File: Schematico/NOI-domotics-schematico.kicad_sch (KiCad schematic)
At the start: 4 parts

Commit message: avanzo
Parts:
- added U?: (no value), symbol USB_5V:USB_DCconverter
- added U?: (no value), symbol Isolator:VO615A-4
- K?: value FINDER-34.51 -> (none)
- U?: value VO615A-4 -> (none)
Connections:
- net at U?. (VCC): now also J?.37 (GPIO26)
- net at J?.18 (GPIO24): now also U?. (VCC)
- net at J?.19 (GPIO10): now also U?. (VCC)
- net at J?.21 (GPIO9): now also U?. (VCC)
- net at J?.22 (GPIO25): now also U?. (VCC)
- net at J?.23 (GPIO11): now also U?. (VCC)
- net at J?.24 (GPIO8): now also U?. (VCC)
- net at J?.26 (GPIO7): now also U?. (VCC)
- net at J?.29 (GPIO5): now also U?. (VCC)
- net at J?.31 (GPIO6): now also U?. (VCC)
- net at J?.32 (GPIO12): now also U?. (VCC)
- net at J?.33 (GPIO13): now also U?. (VCC)
- net at J?.35 (GPIO19): now also U?. (VCC)
- net at J?.36 (GPIO16): now also U?. (VCC)
- net at J?.38 (GPIO20): now also U?. (VCC)
- net at J?.40 (GPIO21): now also U?. (VCC)
- net at K?. (VCC): now also U?.1 (VP)
- new net: K?. (VCC), U?.1 (VP) (x15)
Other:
- moved on the sheet: J?, U?

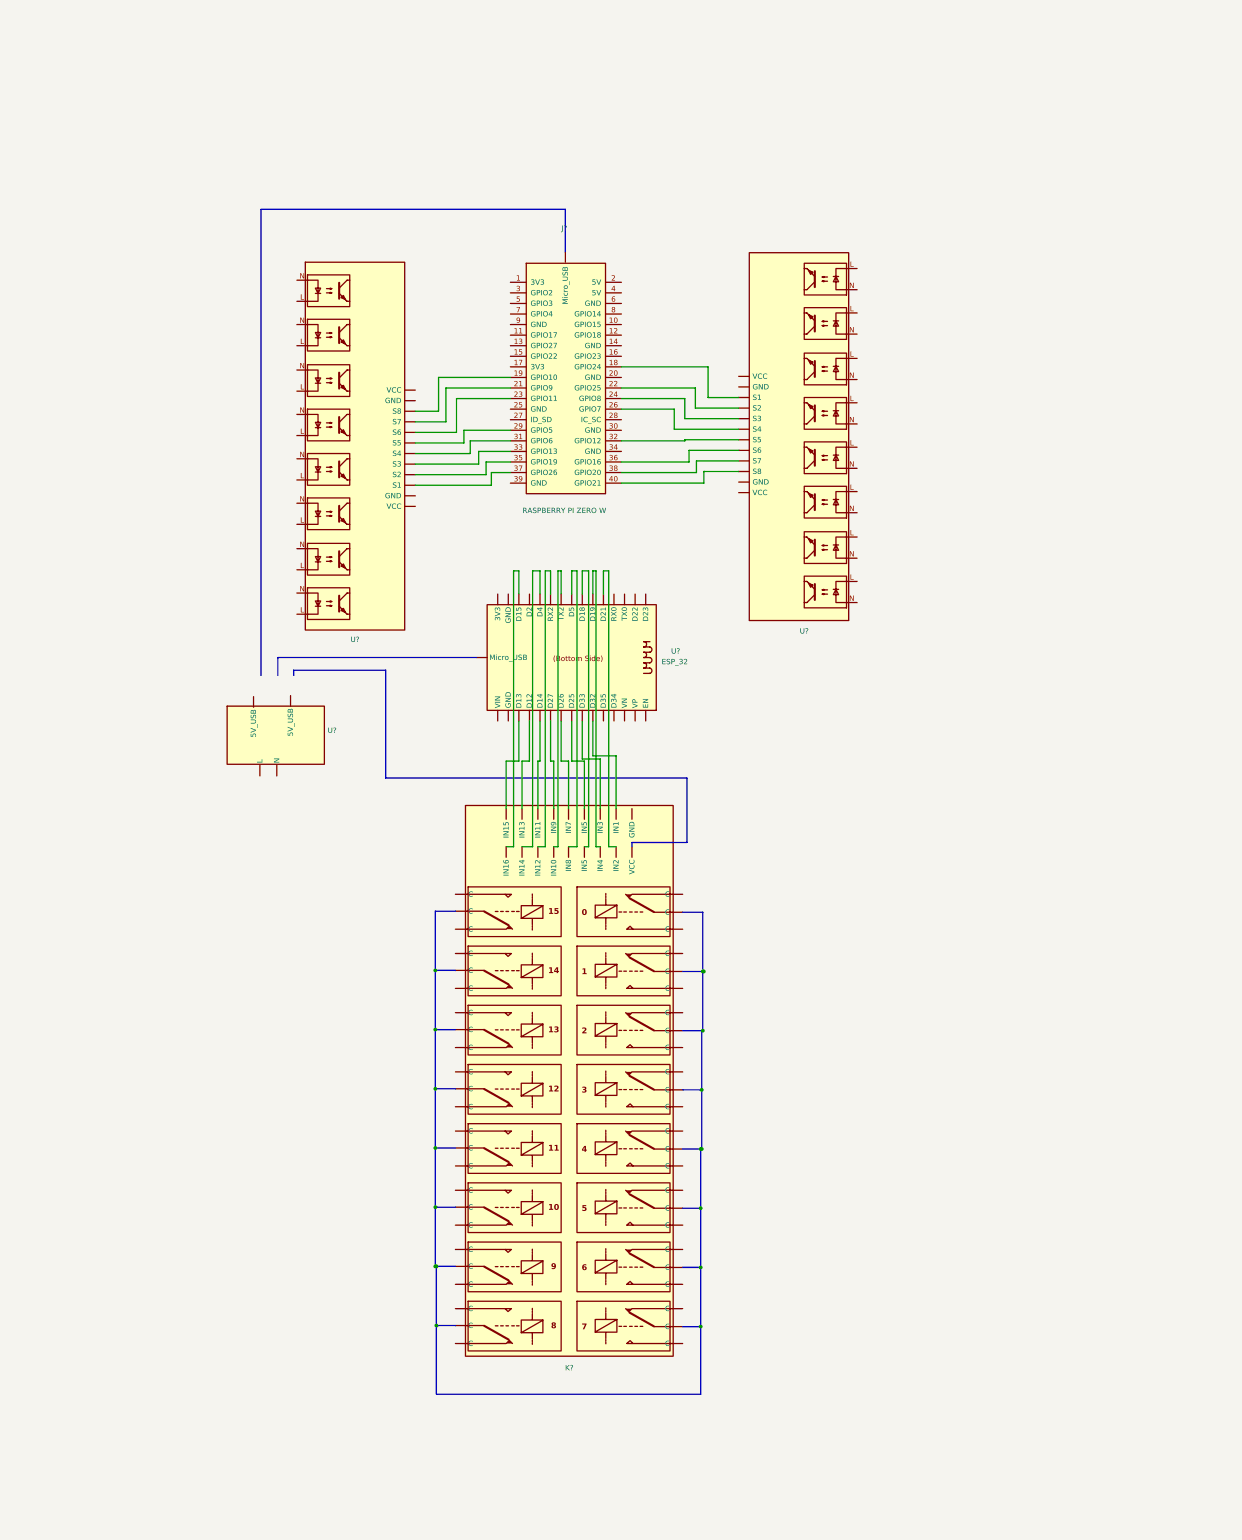
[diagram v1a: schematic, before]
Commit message: updated esp pins
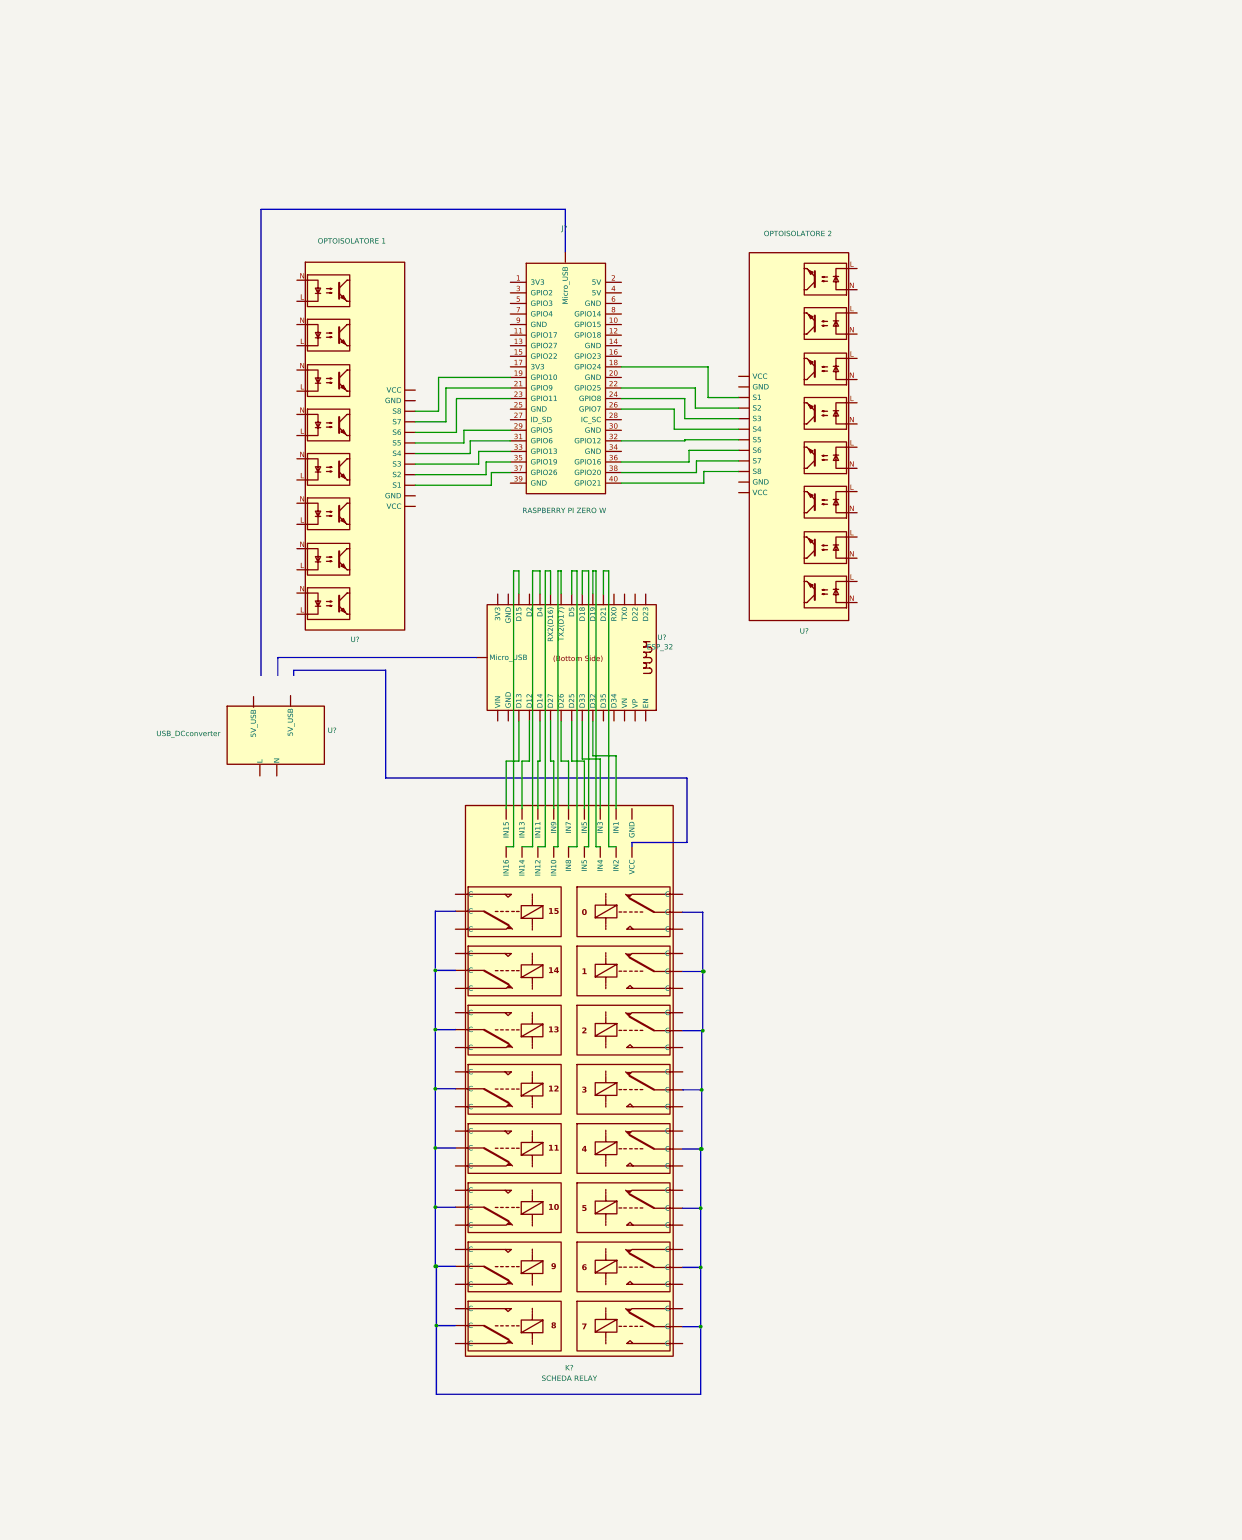
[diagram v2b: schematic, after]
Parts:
- K?: value (none) -> SCHEDA RELAY
- U?: value (none) -> OPTOISOLATORE 1
- U?: value (none) -> USB_DCconverter
- U?: value (none) -> OPTOISOLATORE 2
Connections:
- net at U?. (VCC): now also J?.37 (GPIO26)
- net at K?. (VCC): now also U?.1 (VP)
- net at U?.1 (VP): no longer K?. (VCC)
- new net: K?. (VCC), U?.1 (VP) (x15)
- now unconnected: U?.1 (VP), U?.1 (VP), U?.1 (VP), U?.1 (VP), U?.1 (VP), U?.1 (VP), U?.1 (VP), U?.1 (VP), U?.1 (VP), U?.1 (VP), U?.1 (VP), U?.1 (VP), U?.1 (VP), U?.1 (VP), U?.1 (VP)
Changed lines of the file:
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@@
     (in_bom yes) (on_board yes)
     (property "Reference" "U?" (id 0) (at 96.774 160.274 0))
-    (property "Value" "" (id 1) (at 96.012 64.516 0))
+    (property "Value" "OPTOISOLATORE 1" (id 1) (at 96.012 64.516 0))
     (property "Footprint" "" (id 2) (at 90.424 76.454 0)
       (effects (font (size 1.27 1.27)) hide)
@@
       (effects (font (size 1.27 1.27)) (justify left))
     )
-    (property "Value" "" (id 1) (at 49.022 182.88 0)
+    (property "Value" "USB_DCconverter" (id 1) (at 49.022 182.88 0)
       (effects (font (size 1.27 1.27)) (justify left))
     )
@@
     (in_bom yes) (on_board yes) (fields_autoplaced)
     (property "Reference" "K?" (id 0) (at 148.2725 335.28 0))
-    (property "Value" "" (id 1) (at 148.2725 337.82 0))
+    (property "Value" "SCHEDA RELAY" (id 1) (at 148.2725 337.82 0))
     (property "Footprint" "Relay_THT:Relay_SPDT_Finder_34.51_Vertical" (id 2) (at 172.974 181.864 0)
       (effects (font (size 1.27 1.27)) hide)
@@
   (symbol (lib_id "ESP32:ESP_32") (at 160.274 172.212 270) (mirror x) (unit 1)
     (in_bom yes) (on_board yes)
-    (property "Reference" "U?" (id 0) (at 172.72 163.068 90)
-      (effects (font (size 1.27 1.27)) (justify left))
-    )
-    (property "Value" "ESP_32" (id 1) (at 170.434 165.608 90)
+    (property "Reference" "U?" (id 0) (at 169.418 159.766 90)
+      (effects (font (size 1.27 1.27)) (justify left))
+    )
+    (property "Value" "ESP_32" (id 1) (at 166.878 162.052 90)
       (effects (font (size 1.27 1.27)) (justify left))
     )
@@
     (in_bom yes) (on_board yes)
     (property "Reference" "U?" (id 0) (at 204.724 158.242 0))
-    (property "Value" "" (id 1) (at 203.2 62.738 0))
+    (property "Value" "OPTOISOLATORE 2" (id 1) (at 203.2 62.738 0))
     (property "Footprint" "" (id 2) (at 209.804 148.844 0)
       (effects (font (size 1.27 1.27)) hide)

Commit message: jdjdj
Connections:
- net at U?. (VCC): now also J?.39 (GND)
- net at J?.1 (3V3): now also U?. (VCC)
- net at J?.14 (GND): now also U?. (VCC)
- net at J?.17 (3V3): now also U?. (VCC)
- net at K?. (VCC): now also U?.1 (VP)
- net at U?.1 (VP): no longer K?. (VCC)
- new net: K?. (VCC), U?.1 (VP) (x15)
- now unconnected: U?.1 (VP), U?.1 (VP), U?.1 (VP), U?.1 (VP), U?.1 (VP), U?.1 (VP), U?.1 (VP), U?.1 (VP), U?.1 (VP), U?.1 (VP), U?.1 (VP), U?.1 (VP), U?.1 (VP), U?.1 (VP), U?.1 (VP)
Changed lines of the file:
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@@
+    (stroke (width 0) (type default) (color 0 0 0 0))
+  )
+  (wire (pts (xy 182.88 99.568) (xy 182.88 89.662))
     (stroke (width 0) (type default) (color 0 0 0 0))
   )
@@
     (stroke (width 0) (type default) (color 0 0 0 0))
   )
+  (wire (pts (xy 188.976 99.568) (xy 182.88 99.568))
+    (stroke (width 0) (type default) (color 0 0 0 0))
+  )
   (wire (pts (xy 143.764 179.832) (xy 143.764 189.484))
     (stroke (width 0) (type default) (color 0 0 0 0))
@@
     (stroke (width 0) (type default) (color 0 0 0 0))
   )
+  (wire (pts (xy 131.572 122.682) (xy 131.572 125.73))
+    (stroke (width 0) (type default) (color 0 0 0 0))
+  )
   (wire (pts (xy 136.906 210.058) (xy 139.446 210.058))
     (stroke (width 0) (type default) (color 0 0 0 0))
@@
     (stroke (width 0) (type default) (color 0 0 0 0))
   )
+  (wire (pts (xy 129.794 74.422) (xy 129.794 63.754))
+    (stroke (width 0) (type default) (color 0 0 0 0))
+  )
   (bus (pts (xy 147.32 56.896) (xy 74.168 56.896))
     (stroke (width 0) (type default) (color 0 0 0 0))
@@
     (stroke (width 0) (type default) (color 0 0 0 0))
   )
-  (wire (pts (xy 160.782 94.742) (xy 181.61 94.742))
+  (wire (pts (xy 184.912 63.754) (xy 184.912 97.028))
+    (stroke (width 0) (type default) (color 0 0 0 0))
+  )
+  (wire (pts (xy 160.782 94.742) (xy 180.848 94.742))
     (stroke (width 0) (type default) (color 0 0 0 0))
   )
@@
     (stroke (width 0) (type default) (color 0 0 0 0))
   )
+  (wire (pts (xy 134.112 94.742) (xy 114.554 94.742))
+    (stroke (width 0) (type default) (color 0 0 0 0))
+  )
   (wire (pts (xy 121.158 102.362) (xy 134.112 102.362))
     (stroke (width 0) (type default) (color 0 0 0 0))
@@
     (stroke (width 0) (type default) (color 0 0 0 0))
   )
+  (wire (pts (xy 160.782 89.662) (xy 182.88 89.662))
+    (stroke (width 0) (type default) (color 0 0 0 0))
+  )
   (wire (pts (xy 148.082 210.058) (xy 150.114 210.058))
     (stroke (width 0) (type default) (color 0 0 0 0))
@@
     (stroke (width 0) (type default) (color 0 0 0 0))
   )
+  (wire (pts (xy 131.572 125.73) (xy 111.252 125.73))
+    (stroke (width 0) (type default) (color 0 0 0 0))
+  )
   (wire (pts (xy 136.144 189.484) (xy 133.096 189.484))
     (stroke (width 0) (type default) (color 0 0 0 0))
@@
     (stroke (width 0) (type default) (color 0 0 0 0))
   )
-  (wire (pts (xy 181.61 102.108) (xy 188.976 102.108))
+  (wire (pts (xy 180.848 102.108) (xy 188.976 102.108))
     (stroke (width 0) (type default) (color 0 0 0 0))
   )
@@
     (stroke (width 0) (type default) (color 0 0 0 0))
   )
+  (wire (pts (xy 114.554 100.33) (xy 111.252 100.33))
+    (stroke (width 0) (type default) (color 0 0 0 0))
+  )
   (wire (pts (xy 116.84 97.282) (xy 134.112 97.282))
     (stroke (width 0) (type default) (color 0 0 0 0))
@@
     (stroke (width 0) (type default) (color 0 0 0 0))
   )
+  (wire (pts (xy 184.912 97.028) (xy 188.976 97.028))
+    (stroke (width 0) (type default) (color 0 0 0 0))
+  )
   (wire (pts (xy 155.702 210.058) (xy 154.686 210.058))
     (stroke (width 0) (type default) (color 0 0 0 0))
@@
     (stroke (width 0) (type default) (color 0 0 0 0))
   )
+  (wire (pts (xy 134.112 122.682) (xy 131.572 122.682))
+    (stroke (width 0) (type default) (color 0 0 0 0))
+  )
   (wire (pts (xy 150.114 143.764) (xy 150.114 210.058))
     (stroke (width 0) (type default) (color 0 0 0 0))
@@
     (stroke (width 0) (type default) (color 0 0 0 0))
   )
-  (wire (pts (xy 181.61 94.742) (xy 181.61 102.108))
+  (wire (pts (xy 114.554 94.742) (xy 114.554 100.33))
+    (stroke (width 0) (type default) (color 0 0 0 0))
+  )
+  (wire (pts (xy 180.848 94.742) (xy 180.848 102.108))
+    (stroke (width 0) (type default) (color 0 0 0 0))
+  )
+  (wire (pts (xy 129.794 63.754) (xy 184.912 63.754))
     (stroke (width 0) (type default) (color 0 0 0 0))
   )
@@
   )
   (wire (pts (xy 121.158 110.49) (xy 121.158 102.362))
+    (stroke (width 0) (type default) (color 0 0 0 0))
+  )
+  (wire (pts (xy 134.112 74.422) (xy 129.794 74.422))
     (stroke (width 0) (type default) (color 0 0 0 0))
   )
@@
   (symbol (lib_id "ESP32:ESP_32") (at 160.274 172.212 270) (mirror x) (unit 1)
     (in_bom yes) (on_board yes)
-    (property "Reference" "U?" (id 0) (at 169.418 159.766 90)
+    (property "Reference" "U?" (id 0) (at 173.228 162.306 90)
       (effects (font (size 1.27 1.27)) (justify left))
     )
-    (property "Value" "ESP_32" (id 1) (at 166.878 162.052 90)
+    (property "Value" "ESP_32" (id 1) (at 170.942 166.116 90)
       (effects (font (size 1.27 1.27)) (justify left))
     )
